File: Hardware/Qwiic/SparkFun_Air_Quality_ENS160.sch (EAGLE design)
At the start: 30 parts, among them J1 QWIIC_RIGHT_ANGLE, J2 QWIIC_RIGHT_ANGLE, U1 AP2127K-1.8V

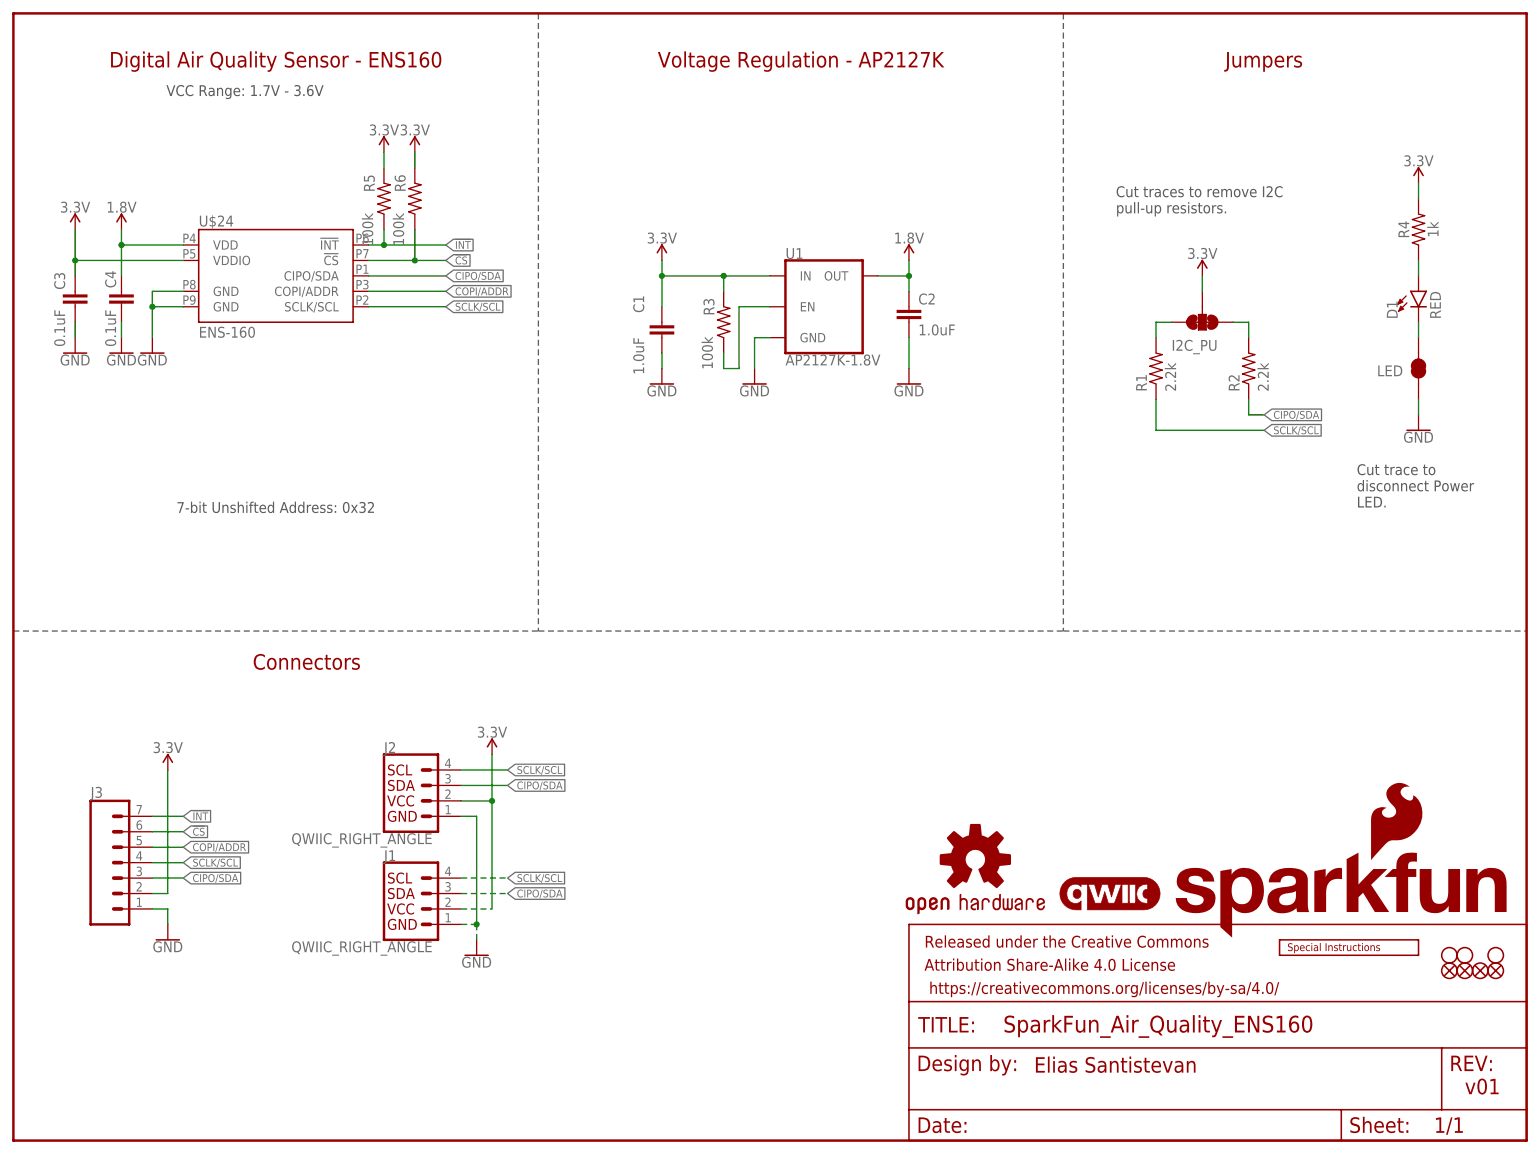
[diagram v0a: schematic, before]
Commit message: Finishes routing, adds silk
* Updates ENS160 symbol to be smaller
* Adds "U" prefix to device
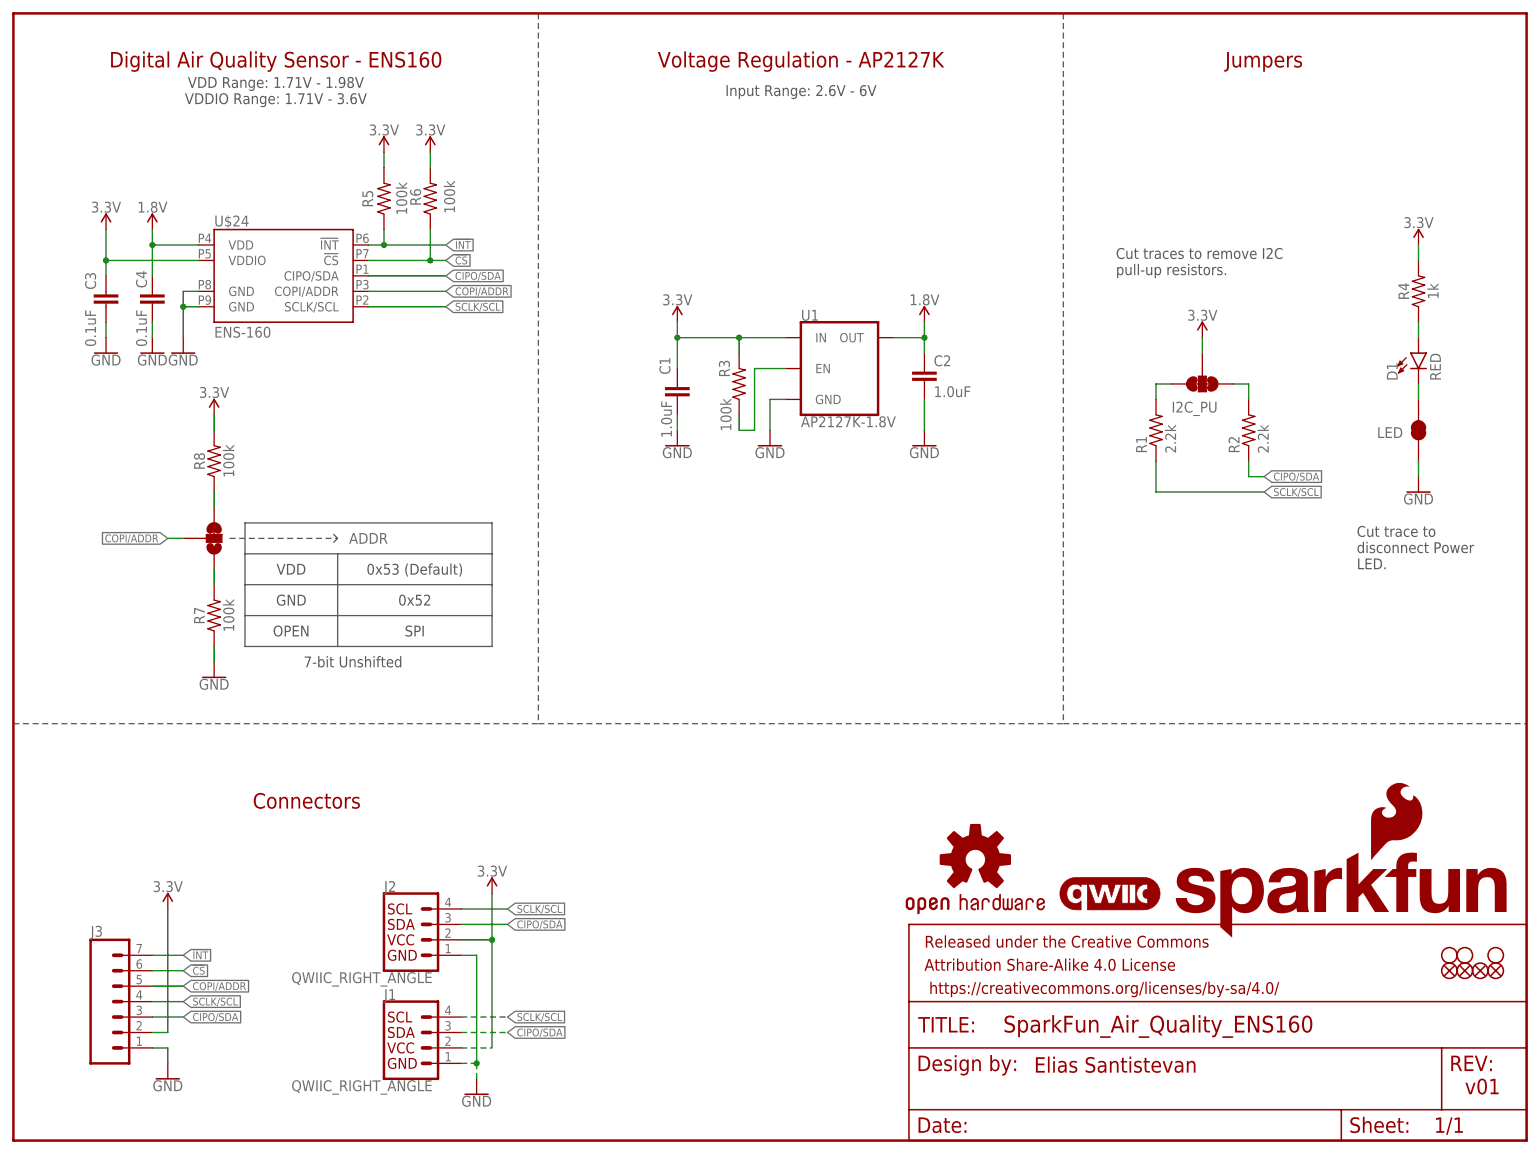
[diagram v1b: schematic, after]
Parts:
- removed LOGO1: SPECIAL_INSTRUCTIONS-PRODUCTION, SparkFun-Aesthetics:SPECIAL_INSTRUCTIONS-PRODUCTION
- added ADDR: JUMPER-SMT_3_1-NC_TRACE_SILK, SparkFun-Jumpers:JUMPER-SMT_3_1-NC_TRACE_SILK
- added R7, R8: 100k, SparkFun-Resistors:100KOHM-0603-1/10W-1%
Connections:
- new net N$4: ADDR.3, R8.1
- new net N$7: ADDR.1, R7.2
- net 3.3V: now also R8.2
- net COPI/ADDR: now also ADDR.2
- net GND: now also R7.1
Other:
- note added: "0x52"
- note added: "0x53 (Default)"
- note added: "7-bit Unshifted"
- note added: "GND"
- note added: "Input Range: 2.6V - 6V"
- note added: "OPEN"
- note added: "SPI"
- note added: "VDD"
- note added: "VDD Range: 1.71V - 1.98V VDDIO Range: 1.71V - 3.6V"
- note removed: "7-bit Unshifted Address: 0x32"
- note removed: "VCC Range: 1.7V - 3.6V"
- moved on the sheet: C1, C2, C3, C4, D1, I2C_PU, J1, J2, J3, LED, R1, R2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

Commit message: Fixes ENS160 symbol to use the correct SPI terminology
* Fixes net names that also used the wrong SPI terminology
* Puts pin one symbol on the correct layer for the ENS160
* Generally fixes ground pour in a number of areas
* Changes version number in schematic
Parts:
- renumbered U$24 to U24
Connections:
- removed net CIPO/SDA: J1.3, J2.3, J3.3, R2.1, U24.CIPO/SDA
- removed net COPI/ADDR: ADDR.2, J3.5, U24.COPI/ADDR
- new net PICO/ADDR: ADDR.2, J3.5, U24.PICO/ADDR
- new net POCI/SDA: J1.3, J2.3, J3.3, R2.1, U24.POCI/SDA
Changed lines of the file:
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@@
 <part name="FD4" library="SparkFun-Aesthetics" deviceset="FIDUCIAL" device="1X2"/>
 <part name="LOGO4" library="SparkFun-Aesthetics" deviceset="QWIIC_LOGO" device="_4MM"/>
-<part name="U$24" library="ENS160" deviceset="ENS-160" device=""/>
+<part name="U24" library="ENS160" deviceset="ENS-160" device=""/>
 <part name="U1" library="SparkFun-IC-Power" deviceset="V_REG_AP2127" device="K-1.8V" value="AP2127K-1.8V"/>
 <part name="C1" library="SparkFun-Capacitors" deviceset="1.0UF" device="-0603-16V-10%" value="1.0uF"/>
@@
 <wire x1="86.36" y1="185.42" x2="86.36" y2="68.58" width="0.2032" layer="97" style="longdash"/>
 <text x="238.76" y="7.62" size="2.54" layer="94" font="vector">v01</text>
-<text x="205.74" y="177.8" size="2.54" layer="94" font="vector" align="center">Jumpers</text>
+<text x="210.82" y="177.8" size="2.54" layer="94" font="vector" align="center">Jumpers</text>
 <text x="220.98" y="93.98" size="1.778" layer="97" font="vector">Cut trace to
 disconnect Power
 LED.</text>
-<text x="48.26" y="55.88" size="2.54" layer="94" font="vector" align="center">Connectors</text>
+<text x="48.26" y="60.96" size="2.54" layer="94" font="vector" align="center">Connectors</text>
 <text x="167.894" y="11.176" size="2.54" layer="94" font="vector">Elias Santistevan</text>
 <text x="43.18" y="177.8" size="2.54" layer="94" font="vector" align="center">Digital Air Quality Sensor - ENS160</text>
@@
 <instance part="FD4" gate="G$1" x="243.84" y="27.94" smashed="yes"/>
 <instance part="LOGO4" gate="G$1" x="180.34" y="40.64" smashed="yes"/>
-<instance part="U$24" gate="G$1" x="43.18" y="142.24" smashed="yes">
+<instance part="U24" gate="G$1" x="43.18" y="142.24" smashed="yes">
 <attribute name="NAME" x="33.02" y="150.368" size="1.778" layer="95" font="vector"/>
 <attribute name="VALUE" x="33.02" y="132.08" size="1.778" layer="96" font="vector"/>
@@
 </segment>
 <segment>
-<pinref part="U$24" gate="G$1" pin="GND@8"/>
+<pinref part="U24" gate="G$1" pin="GND@8"/>
 <wire x1="30.48" y1="139.7" x2="27.94" y2="139.7" width="0.1524" layer="91"/>
 <wire x1="27.94" y1="139.7" x2="27.94" y2="137.16" width="0.1524" layer="91"/>
-<pinref part="U$24" gate="G$1" pin="GND@9"/>
+<pinref part="U24" gate="G$1" pin="GND@9"/>
 <wire x1="27.94" y1="137.16" x2="27.94" y2="132.08" width="0.1524" layer="91"/>
 <wire x1="30.48" y1="137.16" x2="27.94" y2="137.16" width="0.1524" layer="91"/>
@@
 <segment>
 <wire x1="15.24" y1="149.86" x2="15.24" y2="144.78" width="0.1524" layer="91"/>
-<pinref part="U$24" gate="G$1" pin="VDDIO"/>
+<pinref part="U24" gate="G$1" pin="VDDIO"/>
 <wire x1="15.24" y1="144.78" x2="30.48" y2="144.78" width="0.1524" layer="91"/>
 <pinref part="SUPPLY8" gate="G$1" pin="3.3V"/>
@@
 <net name="!INT!" class="0">
 <segment>
-<pinref part="U$24" gate="G$1" pin="!INT!"/>
+<pinref part="U24" gate="G$1" pin="!INT!"/>
 <wire x1="60.96" y1="147.32" x2="58.42" y2="147.32" width="0.1524" layer="91"/>
 <pinref part="R5" gate="G$1" pin="1"/>
@@
 </segment>
 <segment>
-<pinref part="U$24" gate="G$1" pin="VDD"/>
+<pinref part="U24" gate="G$1" pin="VDD"/>
 <wire x1="22.86" y1="149.86" x2="22.86" y2="147.32" width="0.1524" layer="91"/>
 <wire x1="22.86" y1="147.32" x2="30.48" y2="147.32" width="0.1524" layer="91"/>
@@
 </segment>
 </net>
-<net name="COPI/ADDR" class="0">
-<segment>
-<pinref part="U$24" gate="G$1" pin="COPI/ADDR"/>
+<net name="PICO/ADDR" class="0">
+<segment>
+<pinref part="U24" gate="G$1" pin="PICO/ADDR"/>
 <wire x1="71.12" y1="139.7" x2="58.42" y2="139.7" width="0.1524" layer="91"/>
 <label x="71.12" y="139.7" size="1.27" layer="95" font="vector" xref="yes"/>
@@
 <net name="SCLK/SCL" class="0">
 <segment>
-<pinref part="U$24" gate="G$1" pin="SCLK/SCL"/>
+<pinref part="U24" gate="G$1" pin="SCLK/SCL"/>
 <wire x1="71.12" y1="137.16" x2="58.42" y2="137.16" width="0.1524" layer="91"/>
 <label x="71.12" y="137.16" size="1.27" layer="95" font="vector" xref="yes"/>
@@
 </segment>
 </net>
-<net name="CIPO/SDA" class="0">
-<segment>
-<pinref part="U$24" gate="G$1" pin="CIPO/SDA"/>
+<net name="POCI/SDA" class="0">
+<segment>
+<pinref part="U24" gate="G$1" pin="POCI/SDA"/>
 <wire x1="71.12" y1="142.24" x2="58.42" y2="142.24" width="0.1524" layer="91"/>
 <label x="71.12" y="142.24" size="1.27" layer="95" font="vector" xref="yes"/>
@@
 <net name="!CS!" class="0">
 <segment>
-<pinref part="U$24" gate="G$1" pin="!CS!"/>
+<pinref part="U24" gate="G$1" pin="!CS!"/>
 <wire x1="71.12" y1="144.78" x2="68.58" y2="144.78" width="0.1524" layer="91"/>
 <pinref part="R6" gate="G$1" pin="1"/>

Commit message: Updates board to reflect changes in pin numbers
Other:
- note added: "v10"
- note removed: "v01"
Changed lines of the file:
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@@
 <wire x1="172.72" y1="68.58" x2="248.92" y2="68.58" width="0.2032" layer="97" style="longdash"/>
 <wire x1="86.36" y1="185.42" x2="86.36" y2="68.58" width="0.2032" layer="97" style="longdash"/>
-<text x="238.76" y="7.62" size="2.54" layer="94" font="vector">v01</text>
+<text x="238.76" y="7.62" size="2.54" layer="94" font="vector">v10</text>
 <text x="210.82" y="177.8" size="2.54" layer="94" font="vector" align="center">Jumpers</text>
 <text x="220.98" y="93.98" size="1.778" layer="97" font="vector">Cut trace to

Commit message: Updated decoupling cap on VDD
* Updates silk
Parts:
- C4: value 0.1uF -> 10uF; device SparkFun-Capacitors:0.1UF-0603-25V-(+80/-20%) -> SparkFun-Capacitors:10UF-0603-6.3V-20%
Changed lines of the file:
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@@
 <part name="J3" library="SparkFun-Connectors" deviceset="CONN_07" device="NO_SILK"/>
 <part name="C3" library="SparkFun-Capacitors" deviceset="0.1UF" device="-0603-25V-(+80/-20%)" value="0.1uF"/>
-<part name="C4" library="SparkFun-Capacitors" deviceset="0.1UF" device="-0603-25V-(+80/-20%)" value="0.1uF"/>
+<part name="C4" library="SparkFun-Capacitors" deviceset="10UF" device="-0603-6.3V-20%" value="10uF"/>
 <part name="GND6" library="SparkFun-PowerSymbols" deviceset="GND" device=""/>
 <part name="GND8" library="SparkFun-PowerSymbols" deviceset="GND" device=""/>

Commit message: Fixes changes to ENS160
* In a panic I swapped pins rather than change the names on the pins - this has been undone. As a result I went to a previous version of the board and fixed the minor problems previously fixed:
* Fixes general ground pour problems
* Fixes silk
* Adds ADR to top pin
* Rolls version back to v10
* Changes VDD decoupling cap to 10uF - not 0.1uF
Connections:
- removed net PICO/ADDR: ADDR.2, J3.5, U24.PICO/ADDR
- removed net POCI/SDA: J1.3, J2.3, J3.3, R2.1, U24.POCI/SDA
- new net PICO/SDA: J1.3, J2.3, J3.3, R2.1, U24.PICO/SDA
- new net POCI/ADDR: ADDR.2, J3.5, U24.POCI/ADDR
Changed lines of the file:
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@@
 </segment>
 </net>
-<net name="PICO/ADDR" class="0">
+<net name="POCI/ADDR" class="0">
 <segment>
-<pinref part="U24" gate="G$1" pin="PICO/ADDR"/>
+<pinref part="U24" gate="G$1" pin="POCI/ADDR"/>
 <wire x1="71.12" y1="139.7" x2="58.42" y2="139.7" width="0.1524" layer="91"/>
 <label x="71.12" y="139.7" size="1.27" layer="95" font="vector" xref="yes"/>
@@
 </segment>
 </net>
-<net name="POCI/SDA" class="0">
+<net name="PICO/SDA" class="0">
 <segment>
-<pinref part="U24" gate="G$1" pin="POCI/SDA"/>
+<pinref part="U24" gate="G$1" pin="PICO/SDA"/>
 <wire x1="71.12" y1="142.24" x2="58.42" y2="142.24" width="0.1524" layer="91"/>
 <label x="71.12" y="142.24" size="1.27" layer="95" font="vector" xref="yes"/>
